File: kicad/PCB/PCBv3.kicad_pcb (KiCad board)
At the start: 2 copper layers, 80 x 55 mm, 53 parts, among them J1 JST_2mm, J2 JST_2mm, J3 3.5mm, J5 Ventilador, J6 48V IN, J7 3.5mm, J9 Selector_TC4420, Q1 IRL520N, SW1 SW_DIP_x03, U1 XIAO-RP2350-DIP, U2 AP2112K-3.3, U3 TB6612FNG, U4 TC4420

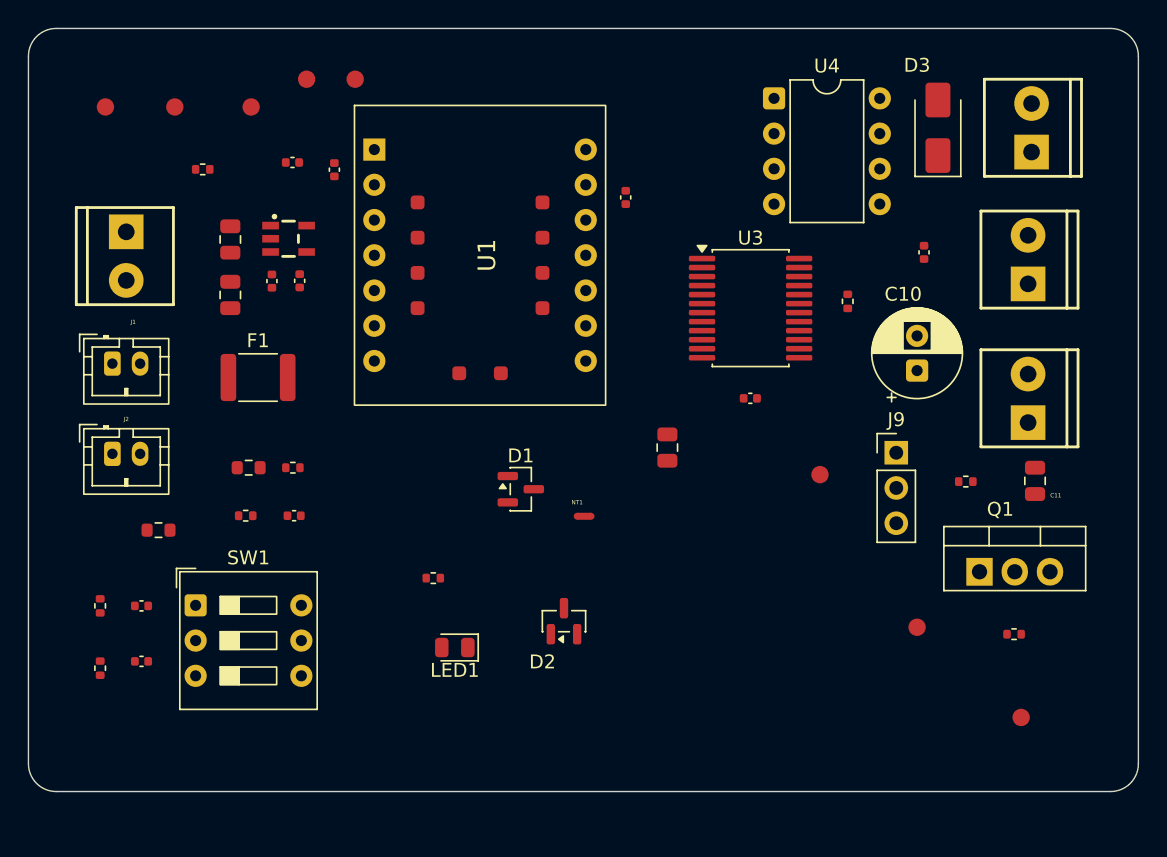
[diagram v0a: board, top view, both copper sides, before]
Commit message: chore: version 1.1.2 - Agregados planos de cobre y organizacion de archivos
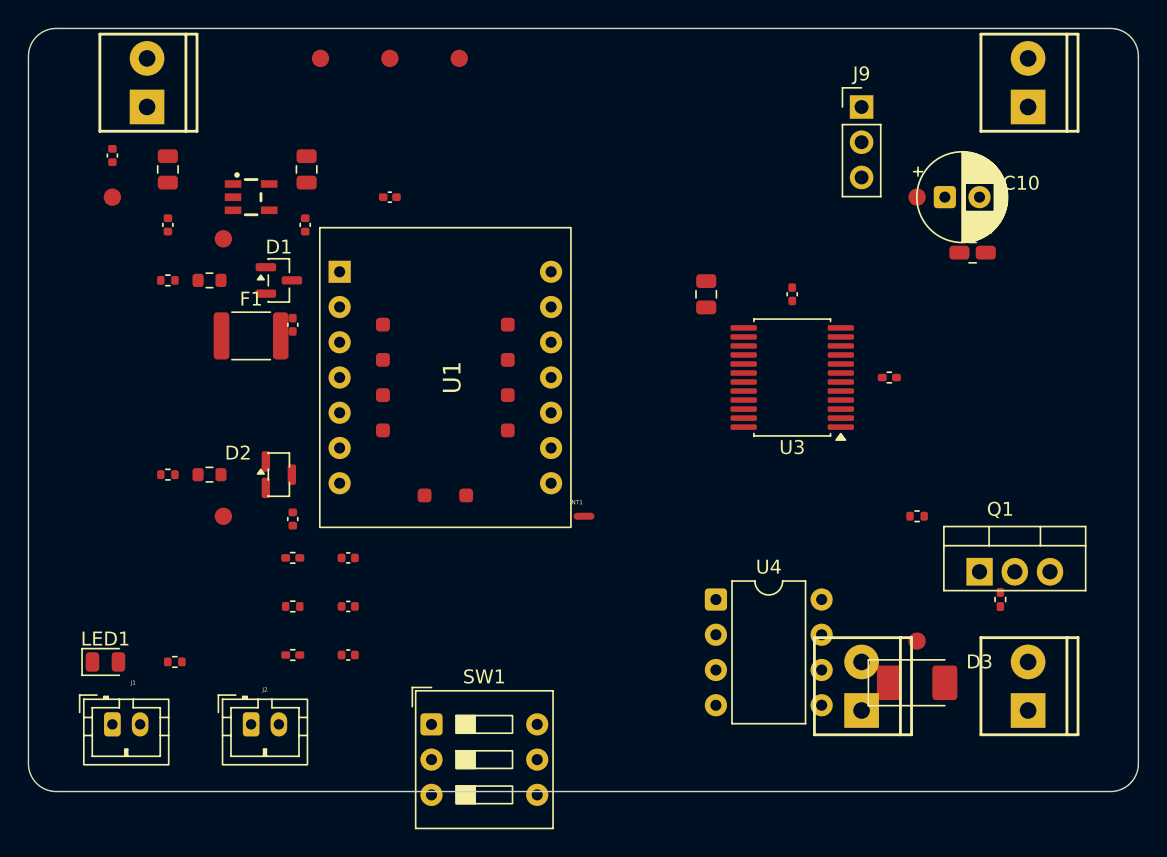
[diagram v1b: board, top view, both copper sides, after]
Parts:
- moved TP4 75.5 mm to (116.0, 82.0)
- moved C15 58.9 mm to (116.0, 79.0), turned to 90 degrees
- moved J5 42.1 mm to (170.0, 119.0)
- moved D3 40.0 mm to (174.0, 117.0), turned to 0 degrees
- moved U4 36.4 mm to (159.5, 111.0)
- moved TP7 32.9 mm to (124.0, 105.0)
- moved J3 30.8 mm to (182.0, 119.0)
- moved J1 26.0 mm to (116.0, 120.0)
- moved C6 25.4 mm to (129.0, 105.2)
- moved LED1 25.2 mm to (115.5, 115.5), turned to 0 degrees
- moved J9 25.0 mm to (170.0, 75.5)
- moved D2 23.1 mm to (128.0, 102.0), turned to 0 degrees
- moved D1 23.0 mm to (128.0, 88.0)
- moved J6 22.8 mm to (182.0, 75.5)
- moved R4 22.1 mm to (120.0, 102.0)
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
